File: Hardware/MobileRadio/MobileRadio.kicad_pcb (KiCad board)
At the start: 2 copper layers, 34 x 98 mm, 0 parts

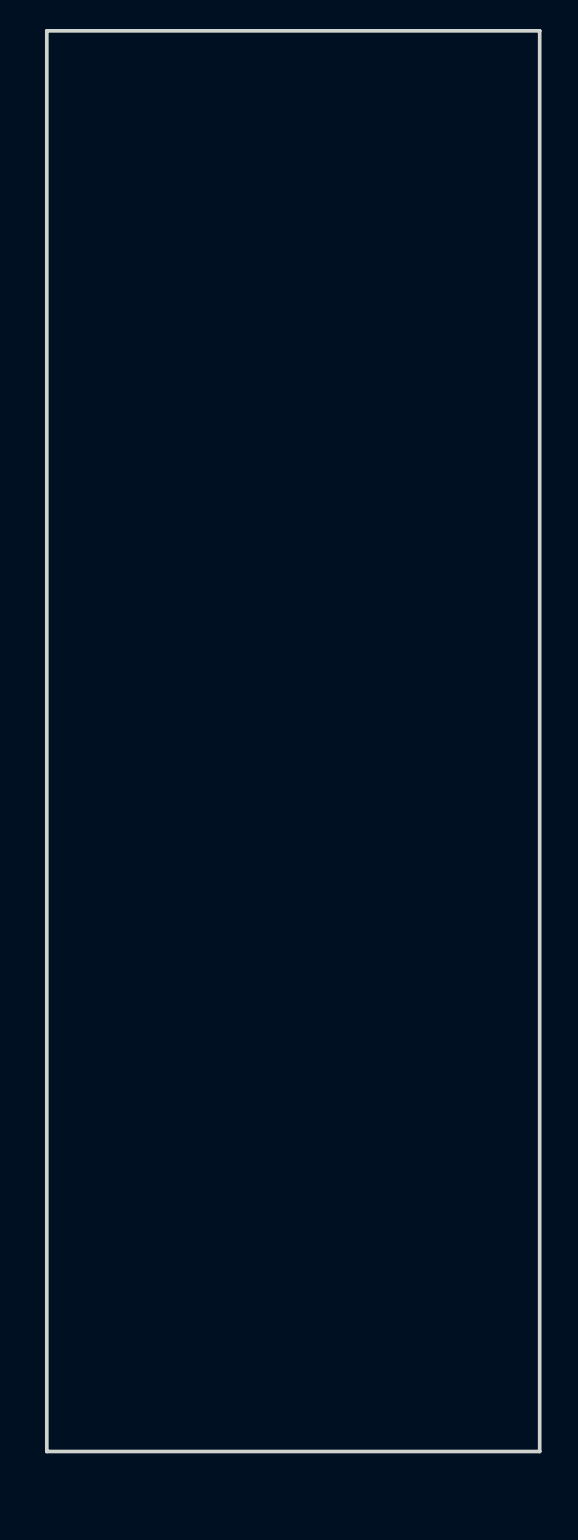
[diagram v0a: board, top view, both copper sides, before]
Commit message: Initial Board Layout - No Audio - No LPF
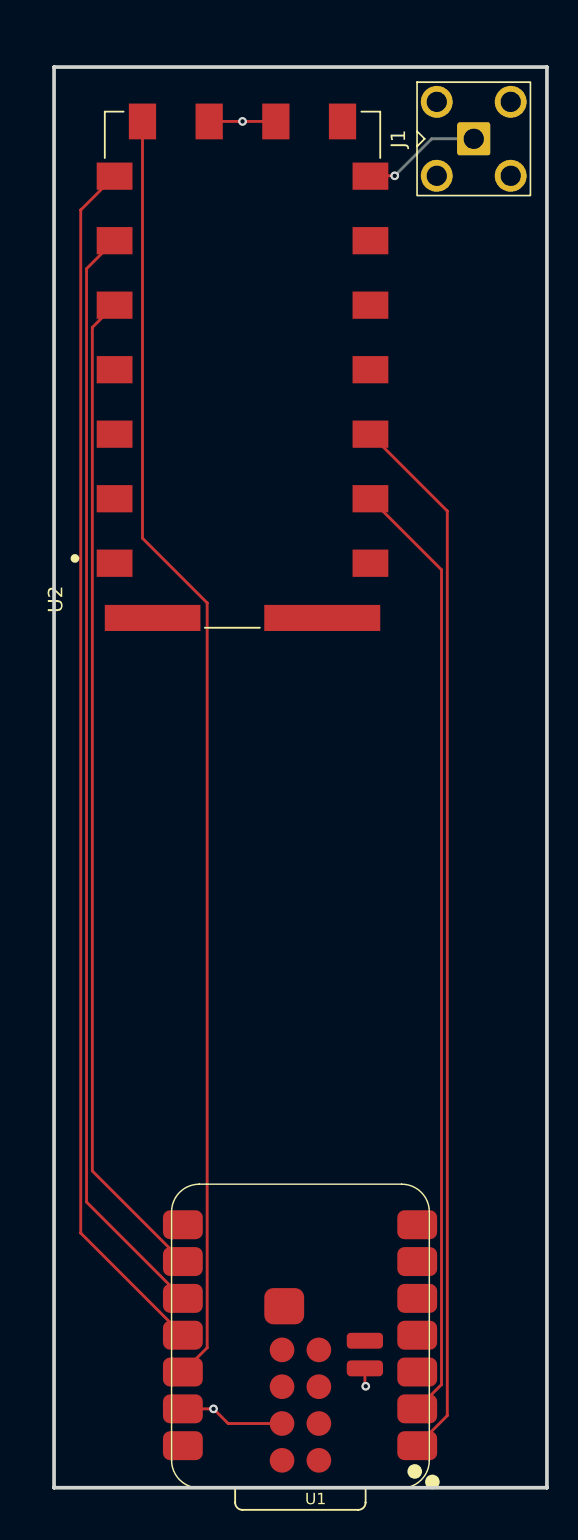
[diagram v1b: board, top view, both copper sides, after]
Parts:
- added J1: Conn_Coaxial, Connector_Coaxial:SMA_BAT_Wireless_BWSMA-KWE-Z001, F.Cu at (128.9, 57.0)
- added U1: XIAO-ESP32-S3-SMD, KiCadFootprints:XIAO-ESP32-S3-SMD_PAD, F.Cu at (125.9, 129.0)
- added U2: DRA818V, KiCadFootprints:DORJI_DRA818V, F.Cu at (113.0, 72.9)
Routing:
- net ESP_3V3: track 0.00 -> 88.8 mm
- net Net-(U1-PA6_A10_D10_MOSI): track 0.00 -> 83.8 mm
- net Net-(U1-PA5_A9_D9_MISO): track 0.00 -> 76.5 mm
- net DRA_RX: track 0.00 -> 72.8 mm
- net Net-(U1-PA7_A8_D8_SCK): track 0.00 -> 69.2 mm
- net DRA_TX: track 0.00 -> 65.5 mm
- net GND: track 0.00 -> 13.9 mm, vias 0 -> 3
- net Net-(J1-In): track 0.00 -> 8.19 mm, vias 0 -> 2
- added copper zone on B.Cu, net GND

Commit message: 4 Layer Board - Isolate the digital from rf & audio
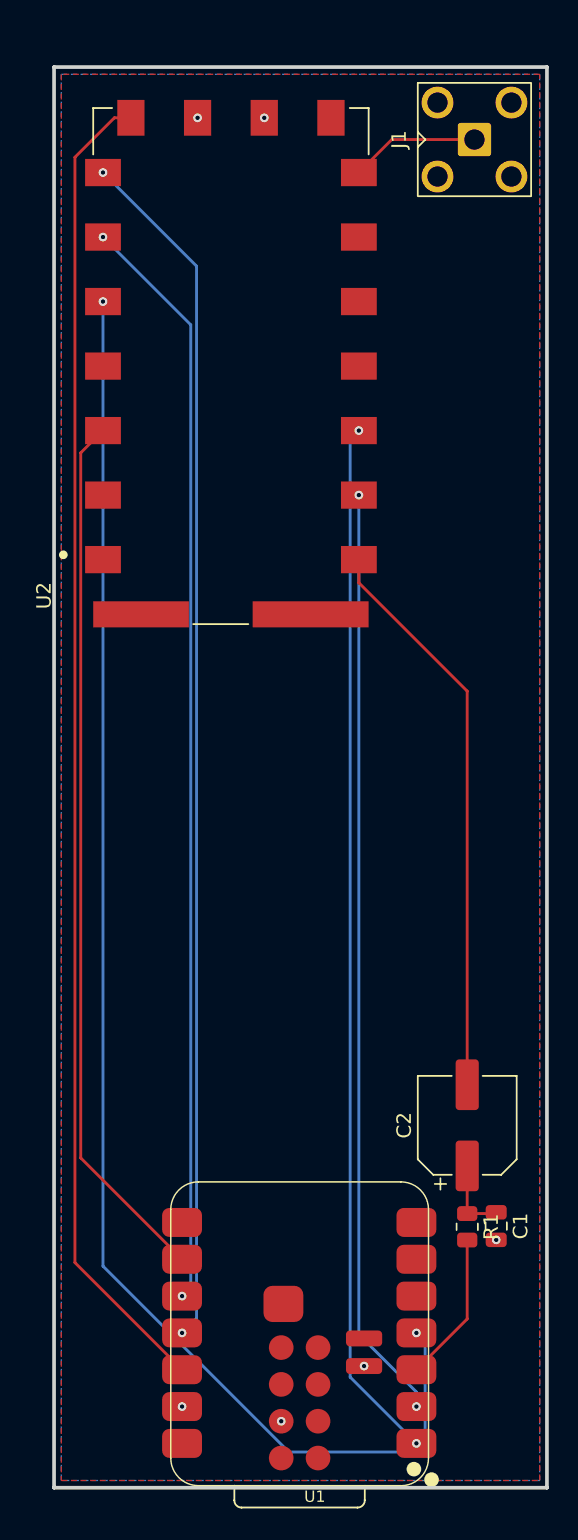
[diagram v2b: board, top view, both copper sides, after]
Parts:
- added C1: 10nF, Capacitor_SMD:C_0805_2012Metric, F.Cu at (130.5, 131.9)
- added C2: 10uF, Capacitor_SMD:CP_Elec_6.3x5.4, F.Cu at (128.5, 125.0)
- added R1: 1K, Resistor_SMD:R_0805_2012Metric, F.Cu at (128.5, 132.0)
- moved U2 0.84 mm to (112.2, 72.6)
- moved U1 0.17 mm to (125.8, 128.8)
- moved J1 0.07 mm to (129.0, 57.0)
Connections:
- U1 pad 3: unconnected-(U1-PA10_A2_D2-Pad3) -> Net-(U1-PA10_A2_D2)
- U1 pad 4: unconnected-(U1-PA11_A3_D3-Pad4) -> Net-(U1-PA11_A3_D3)
- U1 pad 9: Net-(U1-PA7_A8_D8_SCK) -> AF_OUT
- U2 pad 18: unconnected-(U2-MIC_IN-Pad18) -> MIC_IN
- U2 pad 3: unconnected-(U2-AF_OUT-Pad3) -> AF_OUT
- U2 pad 5: Net-(U1-PA7_A8_D8_SCK) -> Net-(U1-PA11_A3_D3)
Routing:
- net Net-(U1-PA11_A3_D3): track 0.00 -> 102.3 mm, vias 0 -> 2
- net Net-(U1-PA7_A8_D8_SCK): track 69.2 -> 0.00 mm
- net AF_OUT: track 0.00 -> 60.7 mm
- net MIC_IN: track 0.00 -> 39.3 mm
- net GND: track 13.9 -> 0.00 mm, vias 3 -> 6
- net Net-(U1-PA10_A2_D2): track 0.00 -> 10.4 mm
- net Net-(C1-Pad1): track 0.00 -> 5.32 mm
- net ESP_3V3: track 88.8 -> 91.7 mm
- net DRA_TX: track 65.5 -> 64.5 mm, vias 0 -> 2
- net DRA_RX: track 72.8 -> 72.0 mm, vias 0 -> 2
- net Net-(J1-In): track 8.19 -> 8.92 mm, vias 2 -> 0
- net Net-(U1-PA6_A10_D10_MOSI): track 83.8 -> 83.1 mm, vias 0 -> 2
- net Net-(U1-PA5_A9_D9_MISO): track 76.5 -> 75.8 mm, vias 0 -> 2
- added copper zone on F.Cu, net GND
- added copper zone on In1.Cu, net GND
- added copper zone on In2.Cu, net GND
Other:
- copper layers 2 -> 4

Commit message: Fix DRC warnings
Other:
- board text added: "U1"
- board text added: "qsldroid v0.0.1 alpha"
